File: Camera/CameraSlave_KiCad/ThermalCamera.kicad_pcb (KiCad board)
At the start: 2 copper layers, 93 x 107 mm, 55 parts, among them J1 I2C, J10 Cam 2, J11 Cam 3, J12 Cam 4, J13 RGB, J14 Fan, J15 I2C, J16 TX PWR Female, J2 XT60 Header, J3 XT60 Header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

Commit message: adding kicad gerbers, PCB and final schematic for REV A
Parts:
- added ?: , , F.Cu at (187.0, 181.5)
- added ?: , , F.Cu at (238.2, 184.8)
- added ?: , , F.Cu at (245.2, 122.8)
- added G***: LOGO, 1FootPrintLibrary:CornLogo, B.Cu at (208.5, 136.5)
- J16: value TX PWR Female -> TX PWR
- J8: value TX -> TX Video
- U4, U5: moved to B.Cu
- moved J13 45.7 mm to (213.8, 191.8)
- moved ? 45.0 mm to (259.8, 93.2)
- moved ? 45.0 mm to (259.0, 191.8)
- moved ? 45.0 mm to (174.0, 93.2)
- moved ? 45.0 mm to (174.0, 191.8)
- moved C1 45.0 mm to (190.8, 103.8)
- moved C10 45.0 mm to (210.9, 147.4)
- moved C11 45.0 mm to (238.1, 170.0)
- moved C2 45.0 mm to (195.0, 105.1)
- moved C3 45.0 mm to (200.6, 148.8)
- moved C4 45.0 mm to (211.0, 105.1)
- moved C5 45.0 mm to (191.2, 166.1)
- moved C6 45.0 mm to (201.5, 121.2)
- moved C7 45.0 mm to (210.8, 126.1)
- moved C8 45.0 mm to (208.0, 166.7)
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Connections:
- ? pad 4: (no net) -> GND (x3)
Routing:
- net GND: track 166.8 -> 405.4 mm, vias 9 -> 0
- net TX Cam 3: track 31.8 -> 67.6 mm, vias 0 -> 1
- net RB1: track 55.6 -> 88.2 mm
- net +13V: track 170.0 -> 146.8 mm
- net TX Cam 4: track 49.5 -> 72.2 mm, vias 0 -> 1
- net RB0: track 71.3 -> 80.6 mm
- net +5V: track 275.0 -> 267.4 mm
- net -5V: track 35.3 -> 41.8 mm
- net RX Cam 3: track 49.5 -> 43.2 mm
- net Net-(U5-OUT): track 12.9 -> 18.8 mm
- net Net-(U3-RC6/TX/CK): track 16.1 -> 10.7 mm, vias 2 -> 1
- net TX Cam 2: track 28.7 -> 33.4 mm, vias 0 -> 3
- net RX Cam 1: track 37.1 -> 33.1 mm
- net RX Cam 2: track 34.4 -> 30.6 mm
- net Net-(U3-RC7/RX/DT): track 12.8 -> 16.3 mm, vias 0 -> 1
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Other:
- board text added: "Camera Control Board Rev A - APRIL 2026 By: Rudy Earnest"

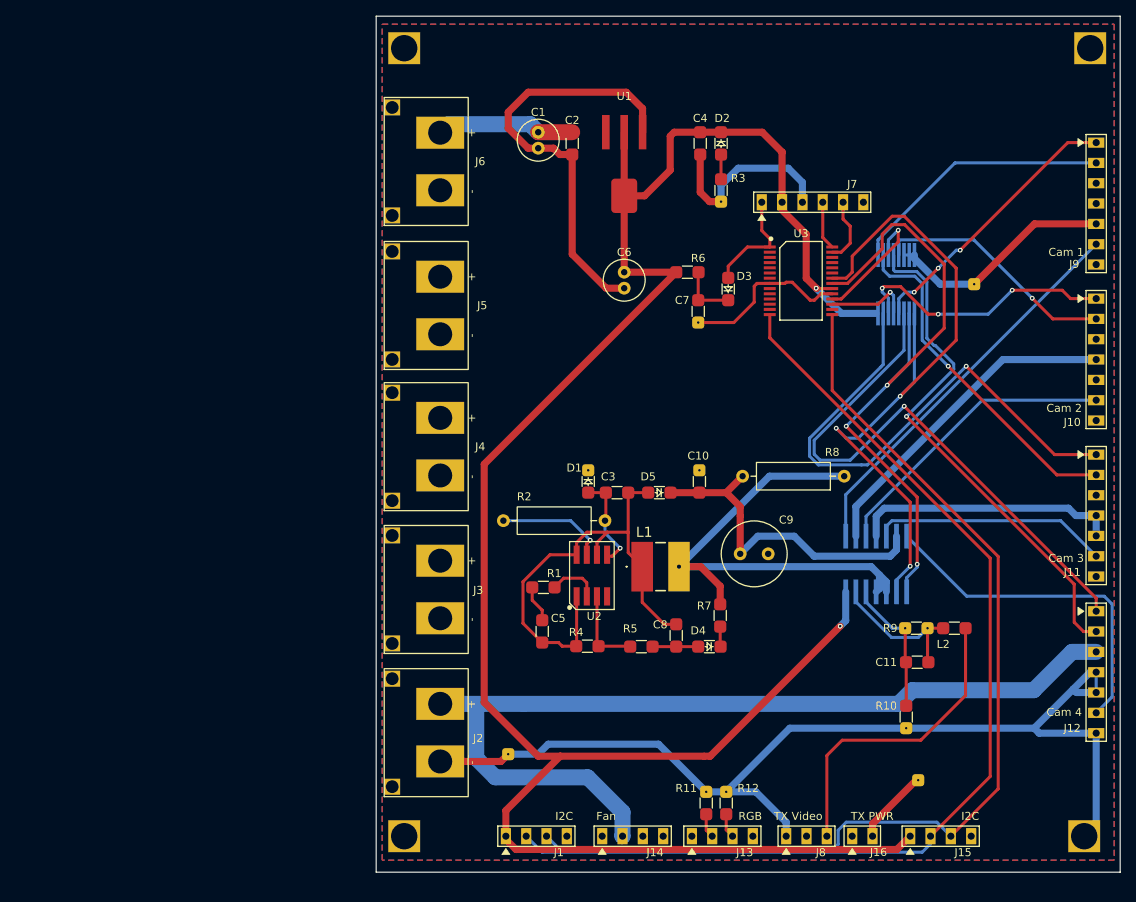
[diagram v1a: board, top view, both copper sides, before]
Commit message: Adding functionality to the zoom for the sony cameras to stop the zoom if it has started, also fixed the homing of the camera
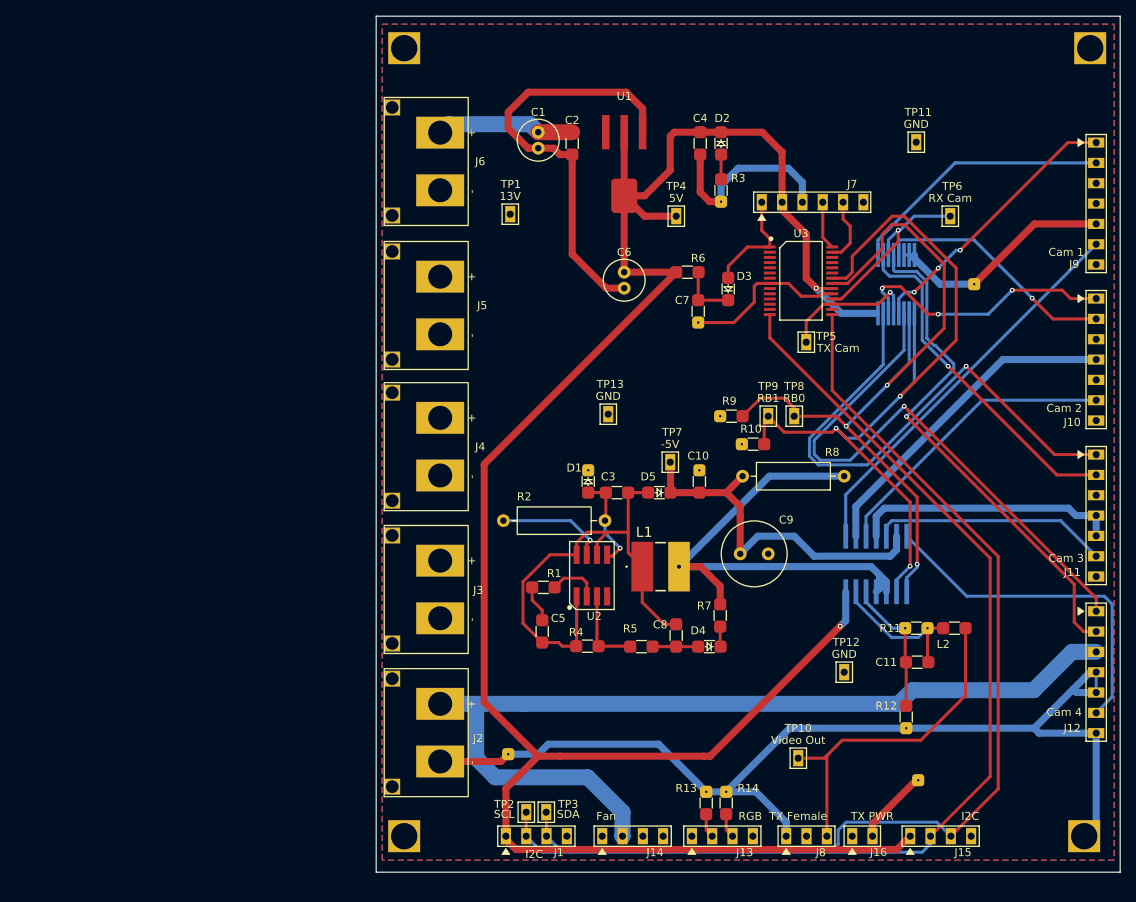
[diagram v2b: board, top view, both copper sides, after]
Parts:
- added R10: 330, 1FootPrintLibrary:0805, F.Cu at (217.6, 142.8)
- added R9: 330, 1FootPrintLibrary:0805, F.Cu at (214.9, 139.2)
- added TP1: 13V, 1FootPrintLibrary:Header_1_x_1, F.Cu at (187.2, 114.0)
- added TP10: Video Out, 1FootPrintLibrary:Header_1_x_1, F.Cu at (223.2, 182.0)
- added TP11: GND, 1FootPrintLibrary:Header_1_x_1, F.Cu at (238.0, 105.0)
- added TP12: GND, 1FootPrintLibrary:Header_1_x_1, F.Cu at (229.0, 171.2)
- added TP13: GND, 1FootPrintLibrary:Header_1_x_1, F.Cu at (199.5, 139.0)
- added TP2: SCL, 1FootPrintLibrary:Header_1_x_1, F.Cu at (189.2, 188.8)
- added TP3: SDA, 1FootPrintLibrary:Header_1_x_1, F.Cu at (191.8, 188.8)
- added TP4: 5V, 1FootPrintLibrary:Header_1_x_1, F.Cu at (208.0, 114.2)
- added TP5: TX Cam, 1FootPrintLibrary:Header_1_x_1, F.Cu at (224.2, 130.0)
- added TP6: RX Cam, 1FootPrintLibrary:Header_1_x_1, F.Cu at (242.2, 114.2)
- added TP7: -5V, 1FootPrintLibrary:Header_1_x_1, F.Cu at (207.2, 145.0)
- added TP8: RB0, 1FootPrintLibrary:Header_1_x_1, F.Cu at (222.8, 139.2)
- added TP9: RB1, 1FootPrintLibrary:Header_1_x_1, F.Cu at (219.5, 139.2)
- J8: value TX Video -> TX Female
- moved G*** 38.5 mm to (220.0, 99.8)
- renumbered R9 to R11, R10 to R12, R11 to R13, R12 to R14
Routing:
- net RB0: track 80.6 -> 96.5 mm
- net RB1: track 88.2 -> 101.5 mm
- net Net-(U3-RC7/RX/DT): track 16.3 -> 23.5 mm
- net Net-(U3-RC6/TX/CK): track 10.7 -> 17.4 mm
- net +5V: track 267.4 -> 273.9 mm
- net -5V: track 41.8 -> 45.6 mm
- net Net-(J8-Pad3): track 38.9 -> 42.7 mm
- net SDA: track 130.4 -> 133.5 mm
- net SCL: track 132.5 -> 135.5 mm
- net GND: track 405.4 -> 404.9 mm
